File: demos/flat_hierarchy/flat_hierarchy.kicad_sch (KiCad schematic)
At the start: 2 parts, among them U7 74LVC1GU04DRL, U8 CD4066BM

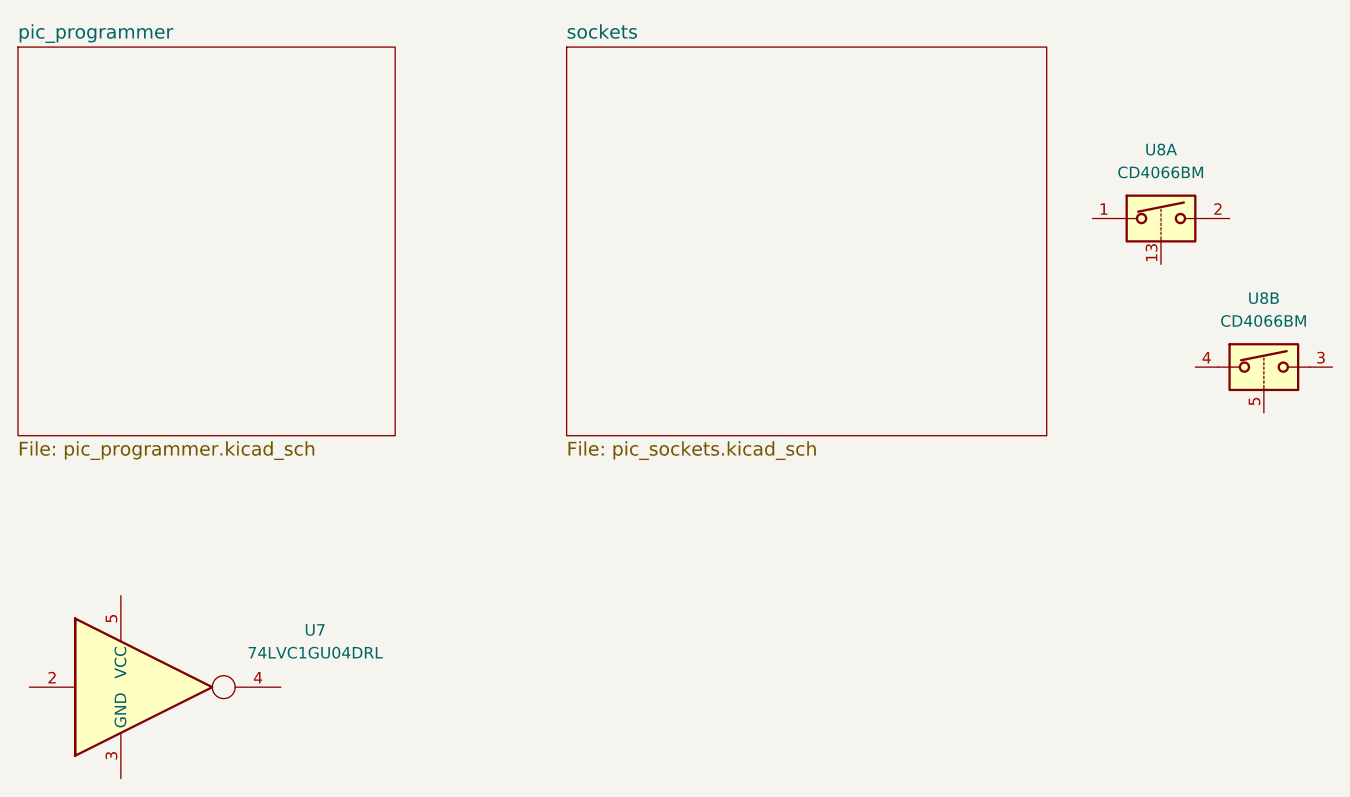
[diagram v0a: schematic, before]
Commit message: Revert : unintended changes in demos project files from commit 903778d6a42e82b62762baea162a9b5c5d8a1b25
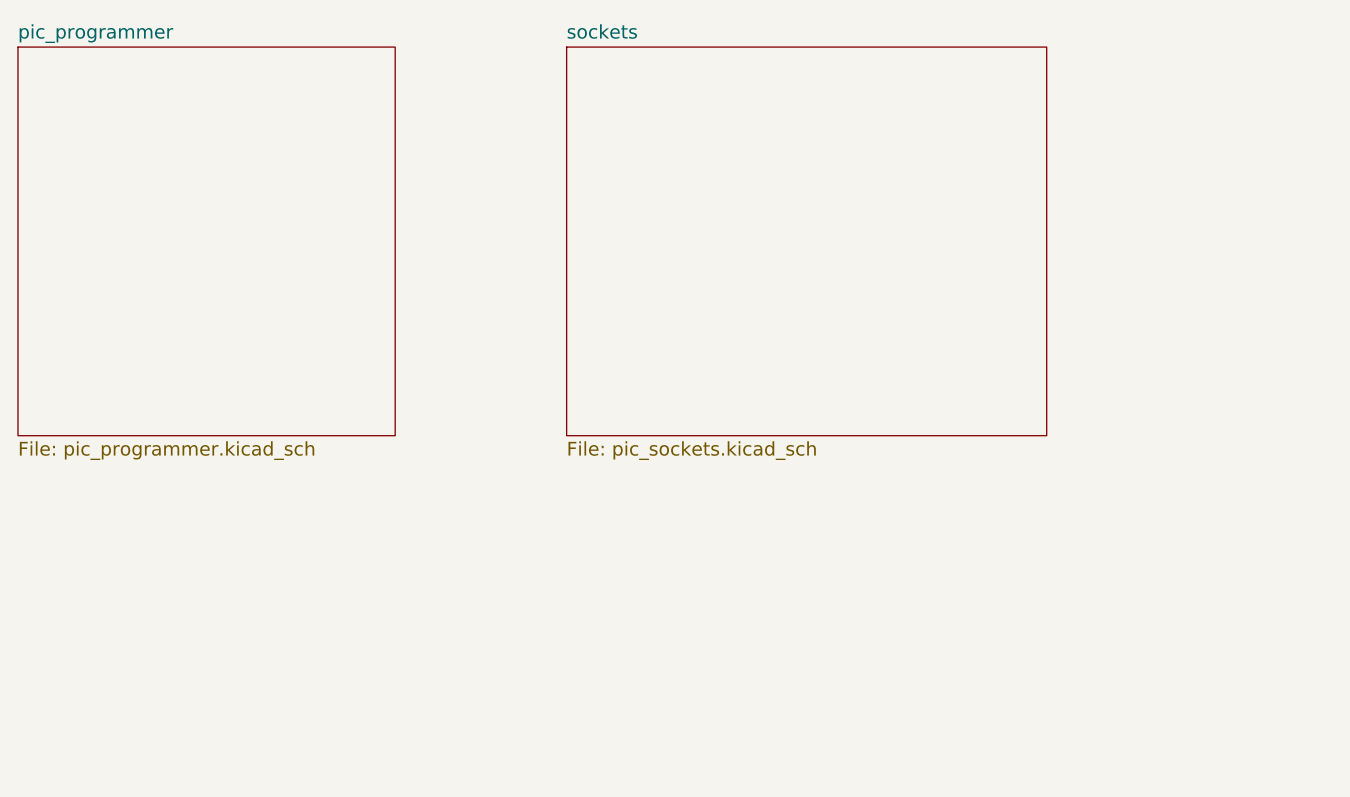
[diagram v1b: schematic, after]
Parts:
- removed U7: 74LVC1GU04DRL, Package_TO_SOT_SMD:SOT-553, symbol 74LVC1GU04DRL:74LVC1GU04DRL
- removed U8: CD4066BM, Package_SO:SO-14_3.9x8.65mm_P1.27mm, symbol CD4066BM:CD4066BM

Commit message: feat: add HQ online parts search panel.
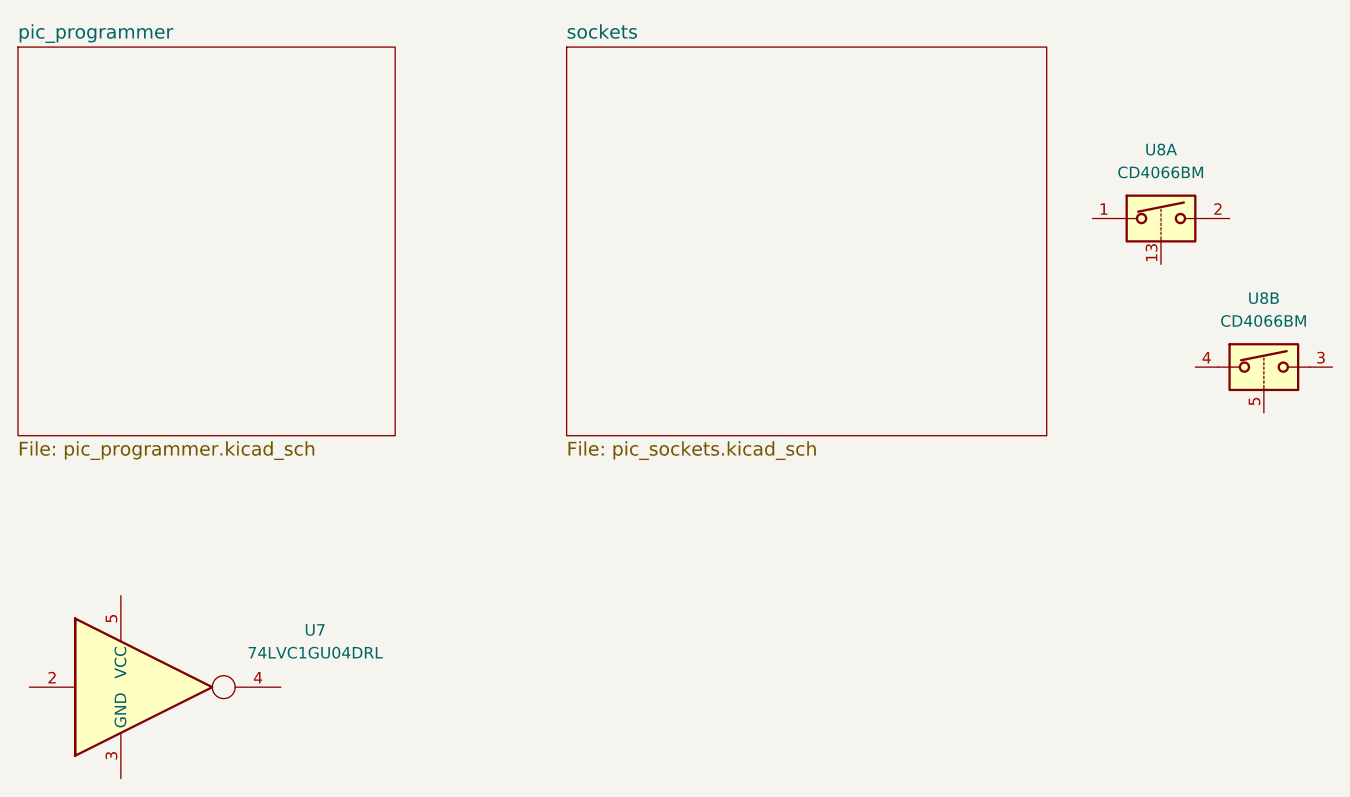
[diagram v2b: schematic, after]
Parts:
- added U7: 74LVC1GU04DRL, Package_TO_SOT_SMD:SOT-553, symbol 74LVC1GU04DRL:74LVC1GU04DRL
- added U8: CD4066BM, Package_SO:SO-14_3.9x8.65mm_P1.27mm, symbol CD4066BM:CD4066BM
